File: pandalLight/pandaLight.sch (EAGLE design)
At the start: 114 parts, among them J1 PJ-037A, U13 TPD12S016PWR, U15 PMOD-2X6, U16 PMOD-2X6, U17 PLR135-T10, U18 PLT133-T10W, U20 TP10SQ, U21 TP10SQ, U22 PAN1322, U23 6SLX9TQG144, U4 FT2232HL, U5 93LC46BT-I/OT, U6 51, U7 51, U8 TPD12S016PWR, X1 USBUB-S, X2 HDMI_RECEPTICAL_A, X4 HDMI_RECEPTICAL_A, Y1 403, Y2 20Mhz

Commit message: Routed PMODs
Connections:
- net PMOD0_0: now also U23B1.IO_L32P_1
- net PMOD0_1: now also U23B1.IO_L33P_1
- net PMOD0_2: now also U23B1.IO_L34P_1
- net PMOD0_3: now also U23B1.IO_L40P_GCLK11_1
- net PMOD1_0: now also U23B1.IO_L1N_VREF_1
- net PMOD1_1: now also U23B1.IO_L32N_1
- net PMOD1_2: now also U23B1.IO_L33N_1
- net PMOD1_3: now also U23B1.IO_L34N_1
- net PMOD2_0: now also U23B0.IO_L62P_0
- net PMOD2_1: now also U23B0.IO_L63P_SCP7_0
- net PMOD2_2: now also U23B0.IO_L64P_SCP5_0
- net PMOD2_3: now also U23B0.IO_L65P_SCP3_0
- net PMOD3_0: now also U23B0.IO_L37N_GCLK12_0
- net PMOD3_1: now also U23B0.IO_L62N_VREF_0
- net PMOD3_2: now also U23B0.IO_L63N_SCP6_0
- net PMOD3_3: now also U23B0.IO_L64N_SCP4_0
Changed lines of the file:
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@@
 </instances>
 <busses>
+<bus name="PMOD2_[0..3],PMOD3_[0..3]">
+<segment>
+<wire x1="50.8" y1="48.26" x2="50.8" y2="30.48" width="0.762" layer="92"/>
+</segment>
+</bus>
 </busses>
 <nets>
@@
 </segment>
 </net>
+<net name="PMOD3_0" class="0">
+<segment>
+<pinref part="U23" gate="B0" pin="IO_L37N_GCLK12_0"/>
+<wire x1="50.8" y1="48.26" x2="25.4" y2="48.26" width="0.1524" layer="91"/>
+<label x="30.48" y="48.26" size="1.778" layer="95"/>
+</segment>
+</net>
+<net name="PMOD2_0" class="0">
+<segment>
+<pinref part="U23" gate="B0" pin="IO_L62P_0"/>
+<wire x1="50.8" y1="45.72" x2="25.4" y2="45.72" width="0.1524" layer="91"/>
+<label x="30.48" y="45.72" size="1.778" layer="95"/>
+</segment>
+</net>
+<net name="PMOD3_1" class="0">
+<segment>
+<pinref part="U23" gate="B0" pin="IO_L62N_VREF_0"/>
+<wire x1="50.8" y1="43.18" x2="25.4" y2="43.18" width="0.1524" layer="91"/>
+<label x="30.48" y="43.18" size="1.778" layer="95"/>
+</segment>
+</net>
+<net name="PMOD2_1" class="0">
+<segment>
+<pinref part="U23" gate="B0" pin="IO_L63P_SCP7_0"/>
+<wire x1="50.8" y1="40.64" x2="25.4" y2="40.64" width="0.1524" layer="91"/>
+<label x="30.48" y="40.64" size="1.778" layer="95"/>
+</segment>
+</net>
+<net name="PMOD3_2" class="0">
+<segment>
+<pinref part="U23" gate="B0" pin="IO_L63N_SCP6_0"/>
+<wire x1="50.8" y1="38.1" x2="25.4" y2="38.1" width="0.1524" layer="91"/>
+<label x="30.48" y="38.1" size="1.778" layer="95"/>
+</segment>
+</net>
+<net name="PMOD2_2" class="0">
+<segment>
+<pinref part="U23" gate="B0" pin="IO_L64P_SCP5_0"/>
+<wire x1="50.8" y1="35.56" x2="25.4" y2="35.56" width="0.1524" layer="91"/>
+<label x="30.48" y="35.56" size="1.778" layer="95"/>
+</segment>
+</net>
+<net name="PMOD3_3" class="0">
+<segment>
+<pinref part="U23" gate="B0" pin="IO_L64N_SCP4_0"/>
+<wire x1="50.8" y1="33.02" x2="25.4" y2="33.02" width="0.1524" layer="91"/>
+<label x="30.48" y="33.02" size="1.778" layer="95"/>
+</segment>
+</net>
+<net name="PMOD2_3" class="0">
+<segment>
+<pinref part="U23" gate="B0" pin="IO_L65P_SCP3_0"/>
+<wire x1="50.8" y1="30.48" x2="25.4" y2="30.48" width="0.1524" layer="91"/>
+<label x="30.48" y="30.48" size="1.778" layer="95"/>
+</segment>
+</net>
 </nets>
 </sheet>
@@
 </instances>
 <busses>
-<bus name="PMOD0_[0..3],PMOD1_[0..3],PMOD2_[0..3],PMOD3_[0..3]">
-<segment>
-<wire x1="195.58" y1="-30.48" x2="195.58" y2="10.16" width="0.762" layer="92"/>
+<bus name="PMOD0_[0..3],PMOD1_[0..3]">
+<segment>
+<wire x1="50.8" y1="50.8" x2="50.8" y2="68.58" width="0.762" layer="92"/>
 </segment>
 </bus>
@@
 </segment>
 </net>
-<net name="BT_RX" class="0">
-<segment>
-<wire x1="185.42" y1="66.04" x2="205.74" y2="66.04" width="0.1524" layer="91"/>
-<label x="187.96" y="66.04" size="1.778" layer="95"/>
-</segment>
-</net>
-<net name="BT_RTS" class="0">
-<segment>
-<wire x1="185.42" y1="73.66" x2="205.74" y2="73.66" width="0.1524" layer="91"/>
-<label x="187.96" y="73.66" size="1.778" layer="95"/>
-</segment>
-</net>
-<net name="BT_CTS" class="0">
-<segment>
-<wire x1="185.42" y1="68.58" x2="205.74" y2="68.58" width="0.1524" layer="91"/>
-<label x="187.96" y="68.58" size="1.778" layer="95"/>
-</segment>
-</net>
-<net name="BT_TX" class="0">
-<segment>
-<wire x1="185.42" y1="71.12" x2="205.74" y2="71.12" width="0.1524" layer="91"/>
-<label x="187.96" y="71.12" size="1.778" layer="95"/>
-</segment>
-</net>
-<net name="BT_WAKE" class="0">
-<segment>
-<wire x1="185.42" y1="63.5" x2="205.74" y2="63.5" width="0.1524" layer="91"/>
-<label x="187.96" y="63.5" size="1.778" layer="95"/>
-</segment>
-</net>
-<net name="BT_RESET#" class="0">
-<segment>
-<wire x1="185.42" y1="60.96" x2="205.74" y2="60.96" width="0.1524" layer="91"/>
-<label x="187.96" y="60.96" size="1.778" layer="95"/>
-</segment>
-</net>
 <net name="LEDS1_CLK_5V" class="0">
 <segment>
@@
 <pinref part="U23" gate="B1" pin="IO_L40N_GCLK10_1"/>
 <label x="30.48" y="48.26" size="1.778" layer="95"/>
+</segment>
+</net>
+<net name="PMOD1_0" class="0">
+<segment>
+<pinref part="U23" gate="B1" pin="IO_L1N_VREF_1"/>
+<wire x1="50.8" y1="68.58" x2="27.94" y2="68.58" width="0.1524" layer="91"/>
+<label x="30.48" y="68.58" size="1.778" layer="95"/>
+</segment>
+</net>
+<net name="PMOD0_0" class="0">
+<segment>
+<pinref part="U23" gate="B1" pin="IO_L32P_1"/>
+<wire x1="50.8" y1="66.04" x2="27.94" y2="66.04" width="0.1524" layer="91"/>
+<label x="30.48" y="66.04" size="1.778" layer="95"/>
+</segment>
+</net>
+<net name="PMOD1_1" class="0">
+<segment>
+<pinref part="U23" gate="B1" pin="IO_L32N_1"/>
+<wire x1="50.8" y1="63.5" x2="27.94" y2="63.5" width="0.1524" layer="91"/>
+<label x="30.48" y="63.5" size="1.778" layer="95"/>
+</segment>
+</net>
+<net name="PMOD0_1" class="0">
+<segment>
+<pinref part="U23" gate="B1" pin="IO_L33P_1"/>
+<wire x1="50.8" y1="60.96" x2="27.94" y2="60.96" width="0.1524" layer="91"/>
+<label x="30.48" y="60.96" size="1.778" layer="95"/>
+</segment>
+</net>
+<net name="PMOD1_2" class="0">
+<segment>
+<pinref part="U23" gate="B1" pin="IO_L33N_1"/>
+<wire x1="50.8" y1="58.42" x2="27.94" y2="58.42" width="0.1524" layer="91"/>
+<label x="30.48" y="58.42" size="1.778" layer="95"/>
+</segment>
+</net>
+<net name="PMOD0_2" class="0">
+<segment>
+<pinref part="U23" gate="B1" pin="IO_L34P_1"/>
+<wire x1="50.8" y1="55.88" x2="27.94" y2="55.88" width="0.1524" layer="91"/>
+<label x="30.48" y="55.88" size="1.778" layer="95"/>
+</segment>
+</net>
+<net name="PMOD1_3" class="0">
+<segment>
+<pinref part="U23" gate="B1" pin="IO_L34N_1"/>
+<wire x1="50.8" y1="53.34" x2="27.94" y2="53.34" width="0.1524" layer="91"/>
+<label x="30.48" y="53.34" size="1.778" layer="95"/>
+</segment>
+</net>
+<net name="PMOD0_3" class="0">
+<segment>
+<pinref part="U23" gate="B1" pin="IO_L40P_GCLK11_1"/>
+<wire x1="50.8" y1="50.8" x2="27.94" y2="50.8" width="0.1524" layer="91"/>
+<label x="30.48" y="50.8" size="1.778" layer="95"/>
 </segment>
 </net>
@@
 </segment>
 </net>
+<net name="BT_RX" class="0">
+<segment>
+<wire x1="53.34" y1="20.32" x2="73.66" y2="20.32" width="0.1524" layer="91"/>
+<label x="55.88" y="20.32" size="1.778" layer="95"/>
+</segment>
+</net>
+<net name="BT_RTS" class="0">
+<segment>
+<wire x1="53.34" y1="27.94" x2="73.66" y2="27.94" width="0.1524" layer="91"/>
+<label x="55.88" y="27.94" size="1.778" layer="95"/>
+</segment>
+</net>
+<net name="BT_CTS" class="0">
+<segment>
+<wire x1="53.34" y1="22.86" x2="73.66" y2="22.86" width="0.1524" layer="91"/>
+<label x="55.88" y="22.86" size="1.778" layer="95"/>
+</segment>
+</net>
+<net name="BT_TX" class="0">
+<segment>
+<wire x1="53.34" y1="25.4" x2="73.66" y2="25.4" width="0.1524" layer="91"/>
+<label x="55.88" y="25.4" size="1.778" layer="95"/>
+</segment>
+</net>
+<net name="BT_WAKE" class="0">
+<segment>
+<wire x1="53.34" y1="17.78" x2="73.66" y2="17.78" width="0.1524" layer="91"/>
+<label x="55.88" y="17.78" size="1.778" layer="95"/>
+</segment>
+</net>
+<net name="BT_RESET#" class="0">
+<segment>
+<wire x1="53.34" y1="15.24" x2="73.66" y2="15.24" width="0.1524" layer="91"/>
+<label x="55.88" y="15.24" size="1.778" layer="95"/>
+</segment>
+</net>

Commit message: Switched 3.3V with ground layer (now ground is on top); Adjusted board width to 90mm; Routed everything, about 10 airwires left!
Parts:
- removed C55, C67, C68, C70, C71: 0.1u, pandaLight:CAPACITOR0402
- removed L4: 47u, pandaLight:INDUCTOR0603
- removed LED2: Yellow, pandaLight:LED0603
- removed R23, R24, R25, R39, R48, R49: 10k, pandaLight:RESISTOR0402
- removed R26: 2.2k, pandaLight:RESISTOR0402
- removed R32: 2.4k, pandaLight:RESISTOR0402
- removed R36: 1k, pandaLight:RESISTOR0402
- removed R37: 4.7k, pandaLight:RESISTOR0402
- removed U$1: M25P40-VMN, pandaLight:M25P40-VMN
- removed U$4: TXB0104RGYR, pandaLight:TXB0104RGYR
- removed U22: PAN1322, pandaLight:PAN1322
- added C15: 0.47u, pandaLight:CAPACITOR0402
- added C16, C19: 0.1u, pandaLight:CAPACITOR0402
- added C17: 4.7u, pandaLight:CAPACITOR0603
- added C18, C23: 27p, pandaLight:CAPACITOR0402
- added L2: 2.2u, 1.3A, pandaLight:INDUCTOR1008
- added R10, R11, R6, R7: 10k, pandaLight:RESISTOR0402
- added R17: 4.7k, pandaLight:RESISTOR0402
- added R2, R3: 100k, pandaLight:RESISTOR0402
- added R4: 1k, pandaLight:RESISTOR0402
- added R9: 12k, pandaLight:RESISTOR0402
- added U12: TPD12S016PWR, pandaLight:TPD12S016PWR
- added U14: PMOD-2X6, pandaLight:PMOD-2X6
- added U3: 93LC46BT-I/OT, pandaLight:93LC46BT-I/OT
- C1, C11: value 0.47u -> 4.7u; device pandaLight:CAPACITOR0402 -> pandaLight:CAPACITOR0603; PARTNO C1005X5R0J474K050BB -> C0603C475K9PACTU
- C12, C32, C37: value 4.7u -> 0.47u; device pandaLight:CAPACITOR0603 -> pandaLight:CAPACITOR0402; PARTNO C0603C475K9PACTU -> C1005X5R0J474K050BB
- C13, C14: value 10u -> 0.47u; device pandaLight:CAPACITOR0603 -> pandaLight:CAPACITOR0402; PARTNO CL10A106MQ8NNNC -> C1005X5R0J474K050BB
- C20, C22, C27, C31, C36, C40, C41: value 0.1u -> 4.7u; device pandaLight:CAPACITOR0402 -> pandaLight:CAPACITOR0603; PARTNO CL05B104KP5NNNC -> C0603C475K9PACTU
- C24, C28, C30, C44, C50: value 4.7u -> 0.1u; device pandaLight:CAPACITOR0603 -> pandaLight:CAPACITOR0402; PARTNO C0603C475K9PACTU -> CL05B104KP5NNNC
- C3: value 4.7u -> 100u; device pandaLight:CAPACITOR0603 -> pandaLight:CAPACITOR1206; PARTNO C0603C475K9PACTU -> CL31A107MQHNNNE
- C33: value 100u -> 0.47u; device pandaLight:CAPACITOR1206 -> pandaLight:CAPACITOR0402; PARTNO CL31A107MQHNNNE -> C1005X5R0J474K050BB
- C34, C35: value 27p -> 0.1u; PARTNO CL05C270JB5NNNC -> CL05B104KP5NNNC
- C4: value 0.47u -> 100u; device pandaLight:CAPACITOR0402 -> pandaLight:CAPACITOR1206; PARTNO C1005X5R0J474K050BB -> CL31A107MQHNNNE
- C42, C43: value 0.1u -> 0.47u; PARTNO CL05B104KP5NNNC -> C1005X5R0J474K050BB
- C45, C46, C51, C52: value 0.47u -> 0.1u; PARTNO C1005X5R0J474K050BB -> CL05B104KP5NNNC
- C5: value 4.7u -> 10u; PARTNO C0603C475K9PACTU -> CL10A106MQ8NNNC
- C6: value 100u -> 10u; device pandaLight:CAPACITOR1206 -> pandaLight:CAPACITOR0603; PARTNO CL31A107MQHNNNE -> CL10A106MQ8NNNC
- JP2: value PMOD0-1_VCC_SEL -> PMOD2-3_VCC_SEL
- JP3: value PMOD2-3_VCC_SEL -> PMOD0-1_VCC_SEL
- L3: value 2.2u, 1.3A -> 47u; device pandaLight:INDUCTOR1008 -> pandaLight:INDUCTOR0603; PARTNO CIG22E1R0MNE -> GLFR1608T470M-LR
- R1: value 1k -> 100k; PARTNO ERJ-2RKF1001X -> ERJ-2RKF1003X
- R16, R5: value 100k -> 10k; PARTNO ERJ-2RKF1003X -> ERJ-2RKF1002X
- R20: value 10k -> 2.4k; PARTNO ERJ-2RKF1002X -> ERJ-2RKF2401X
- R21: value 12k -> 4.7k; PARTNO ERJ-2RKF1202X -> ERJ-2RKF1002X
- R8: value 100k -> 2.2k; PARTNO ERJ-2RKF1003X -> ERJ-2RKF2201X
- U13: value TPD12S016PWR -> M25P40-VMN; device pandaLight:TPD12S016PWR -> pandaLight:M25P40-VMN; PARTNO TPD12S016PWR -> M25P40-VMN6PB
- U16: value PMOD-2X6 -> PLR135-T10; device pandaLight:PMOD-2X6 -> pandaLight:PLR135-T10; PARTNO PPTC062LJBN-RC -> PLR135/T10
- U17: value PLR135-T10 -> PLT133-T10W; device pandaLight:PLR135-T10 -> pandaLight:PLT133-T10W; PARTNO PLR135/T10 -> PLT133/T10W
- U18: value PLT133-T10W -> TP10SQ; device pandaLight:PLT133-T10W -> pandaLight:TP10SQ; BOM (none) -> EXCLUDE; PARTNO PLT133/T10W -> *
- U20: value TP10SQ -> PAN1322; device pandaLight:TP10SQ -> pandaLight:PAN1322; BOM EXCLUDE -> (none); PARTNO * -> ENW-89841A3KF
- U5: value 93LC46BT-I/OT -> TPD12S016PWR; device pandaLight:93LC46BT-I/OT -> pandaLight:TPD12S016PWR; PARTNO 93LC46BT-I/OT -> TPD12S016PWR
- U8: value TPD12S016PWR -> TXB0104RGYR; device pandaLight:TPD12S016PWR -> pandaLight:TXB0104RGYR; PARTNO TPD12S016PWR -> (none)
- renumbered C56 to C47, C57 to C48, C58 to C49, LEDS_CON0 to U11, LEDS_CON1 to U10, R27 to R12, R28 to R13, R29 to R14, R34 to R19, R38 to R18, R40 to R15, U$2 to U1, U$3 to U9, U21 to U19, U23 to U2, X4 to X3
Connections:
- removed net +1V5: C47.1, C48.1, C49.1, U2B3.VCCO_3@0, U2B3.VCCO_3@1, U2B3.VCCO_3@2
- removed net N$33: LED2.C, U2B2.DONE_2
- removed net N$38: LED2.A, R36.1
- net +1V2: now also C10.1, C12.1, C6.1, C8.1, L1.2; no longer C2.1, C3.1, C4.1, L3.2
- net +1V8: now also C28.1, C29.1, C30.1; no longer C24.1, C25.1, C26.1
- net +3V3: now also C15.1, C16.1, C24.1, C25.1, C26.1, C31.1, C33.1, C35.1, C41.1, C47.1, C48.1, C49.1, C53.1, C54.1, C7.1, L2.2, L3.1, R1.1, R10.1, R11.2, R17.2, R20.2, R5.2, R6.2, R7.2, U12.VCCA, U13.HOLD#, U13.VCC, U13.W#, U17.VCC, U20.ONOFF, U20.VDD1, U20.VDDUART, U20.VSUPPLY@A4, U20.VSUPPLY@A5, U20.VSUPPLY@A6, U2B3.VCCO_3@0, U2B3.VCCO_3@1, U2B3.VCCO_3@2, U3.VCC, U5.VCCA, U8.OE; no longer C10.1, C12.1, C20.1, C21.1, C39.1, C44.1, C46.1, C51.1, C55.1, C68.1, C70.1, C71.1, L1.2, L4.1, R16.1, R20.1, R23.2, R24.2, R25.2, R32.2, R36.2, R37.2, R48.2, U$1.HOLD#, U$1.VCC, U$1.W#, U$4.OE, U$4.VCCA, U13.VCCA, U18.VCC, U22.ONOFF, U22.VDD1, U22.VDDUART, U22.VSUPPLY@A4, U22.VSUPPLY@A5, U22.VSUPPLY@A6, U5.VCC
- net +5V: now also C2.1, C34.1, C39.1, C4.1, C40.1, C44.1, R2.1, R3.1, R4.2, U12.VCC5V, U5.VCC5V, U8.VCCB; no longer C41.1, C54.1, C7.1, C8.1, R1.2, R5.1, R8.1, U$4.VCCB, U13.VCC5V, U8.VCC5V
- net 5V_SUP: now also C3.1; no longer C6.1
- net BT_CTS: now also U20.P0.7_UARTCTS, U2B3.IO_L2N_3; no longer U22.P0.7_UARTCTS
- net BT_RESET#: now also R21.2, U20.RESET#, U2B3.IO_L49N_3; no longer R49.2, U22.RESET#
- net BT_RTS: now also U20.P0.6_UARTRTS, U2B3.IO_L1N_VREF_3; no longer U22.P0.6_UARTRTS
- net BT_RX: now also U20.P0.5_UARTRXD, U2B3.IO_L36P_3; no longer U22.P0.5_UARTRXD
- net BT_TX: now also U20.P0.4_UARTTXD, U2B3.IO_L2P_3; no longer U22.P0.4_UARTTXD
- net BT_WAKE: now also R22.1, U20.P0.14_LPMIN, U2B3.IO_L36N_3; no longer R48.1, U22.P0.14_LPMIN
- net FPGA_CLK20: now also U2B3.IO_L83P_3; no longer U2B3.IO_L42N_GCLK24_3
- net GND: now also C15.2, C16.2, C17.2, C18.2, C19.2, C23.2, R16.1, R9.1, U12.GND@0, U12.GND@1, U12.GND@2, U13.VSS, U14.11, U14.5, U16.GND, U20.VSS@A1, U20.VSS@A11, U20.VSS@A12, U20.VSS@A7, U20.VSS@A9, U20.VSS@C8, U20.VSS@C9, U20.VSS@D7, U20.VSS@D8, U20.VSS@E8, U20.VSS@E9, U20.VSS@F1, U20.VSS@F11, U20.VSS@F12, U20.VSS@F9, U3.VSS, U5.GND@0, U5.GND@1, U5.GND@2, U8.EP, U8.GND; no longer C55.2, C67.2, C68.2, C70.2, C71.2, R39.1, R49.1, U$1.VSS, U$4.EP, U$4.GND, U13.GND@0, U13.GND@1, U13.GND@2, U16.11, U16.5, U18.GND, U22.VSS@A1, U22.VSS@A11, U22.VSS@A12, U22.VSS@A7, U22.VSS@A9, U22.VSS@C8, U22.VSS@C9, U22.VSS@D7, U22.VSS@D8, U22.VSS@E8, U22.VSS@E9, U22.VSS@F1, U22.VSS@F11, U22.VSS@F12, U22.VSS@F9, U5.VSS, U8.GND@0, U8.GND@1, U8.GND@2
- net HDMI_RX_5V: now also U5.5V_OUT; no longer C40.1, U8.5V_OUT
- net HDMI_RX_CEC: now also U5.CEC_B; no longer U8.CEC_B
- net HDMI_RX_CEC_3V3: now also U5.CEC_A; no longer U8.CEC_A
- net HDMI_RX_CLK_N: now also U5.CLK-; no longer U8.CLK-
- net HDMI_RX_CLK_P: now also U5.CLK+; no longer U8.CLK+
- net HDMI_RX_CTRL_EN: now also U5.CT_HPD, U5.LS_OE; no longer U8.CT_HPD, U8.LS_OE
- net HDMI_RX_DATA0_N: now also U5.D0-; no longer U8.D0-
- net HDMI_RX_DATA0_P: now also U5.D0+; no longer U8.D0+
- net HDMI_RX_DATA1_N: now also U5.D1-; no longer U8.D1-
- net HDMI_RX_DATA1_P: now also U5.D1+; no longer U8.D1+
- net HDMI_RX_DATA2_N: now also U5.D2-; no longer U8.D2-
- net HDMI_RX_DATA2_P: now also U5.D2+; no longer U8.D2+
- net HDMI_RX_SCL_3V3: now also U5.SCL_A; no longer U8.SCL_A
- net HDMI_RX_SCL_5V: now also U5.SCL_B; no longer U8.SCL_B
- net HDMI_RX_SDA_3V3: now also U5.SDA_A; no longer U8.SDA_A
- net HDMI_RX_SDA_5V: now also U5.SDA_B; no longer U8.SDA_B
- net HDMI_TX_5V: now also C46.1, U12.5V_OUT; no longer C53.1, U13.5V_OUT
- net HDMI_TX_CEC: now also U12.CEC_B; no longer U13.CEC_B
- net HDMI_TX_CEC_3V3: now also U12.CEC_A; no longer U13.CEC_A
- net HDMI_TX_CLK_N: now also U12.CLK-; no longer U13.CLK-
- net HDMI_TX_CLK_P: now also U12.CLK+; no longer U13.CLK+
- net HDMI_TX_CTRL_EN: now also R16.2, U12.CT_HPD, U12.LS_OE; no longer R39.2, U13.CT_HPD, U13.LS_OE
- net HDMI_TX_DATA0_N: now also U12.D0-; no longer U13.D0-
- net HDMI_TX_DATA0_P: now also U12.D0+; no longer U13.D0+
- net HDMI_TX_DATA1_N: now also U12.D1-; no longer U13.D1-
- net HDMI_TX_DATA1_P: now also U12.D1+; no longer U13.D1+
- net HDMI_TX_DATA2_N: now also U12.D2-; no longer U13.D2-
- net HDMI_TX_DATA2_P: now also U12.D2+; no longer U13.D2+
- net HDMI_TX_HPD_5V: now also U12.HPD_B; no longer U13.HPD_B
- net HDMI_TX_SCL_3V3: now also U12.SCL_A; no longer U13.SCL_A
- net HDMI_TX_SCL_5V: now also U12.SCL_B; no longer U13.SCL_B
- net HDMI_TX_SDA_3V3: now also U12.SDA_A; no longer U13.SDA_A
- net HDMI_TX_SDA_5V: now also U12.SDA_B; no longer U13.SDA_B
- net LEDS0_CLK: now also U8.A4; no longer U$4.A4
- net LEDS0_CLK_5V: now also U8.B4; no longer U$4.B4
- net LEDS0_DATA: now also U8.A1; no longer U$4.A1
- net LEDS0_DATA_5V: now also U8.B1; no longer U$4.B1
- net LEDS1_CLK: now also U8.A2; no longer U$4.A2
- net LEDS1_CLK_5V: now also U8.B2; no longer U$4.B2
- net LEDS1_DATA: now also U8.A3; no longer U$4.A3
- net LEDS1_DATA_5V: now also U8.B3; no longer U$4.B3
- net N$1: now also C23.1; no longer C35.1
- net N$10: now also R8.2, U3.DI; no longer R26.2, U5.DI
- net N$11: now also R9.2; no longer R21.2
- net N$12: now also R7.1, R8.1, U3.DO; no longer R25.1, R26.1, U5.DO
- net N$13: now also R10.2; no longer R20.2
- net N$19: now also U20.P0.12_SDA0; no longer U22.P0.12_SDA0
- net N$25: now also R3.2; no longer R8.2
- net N$27: now also R1.2; no longer R16.2
- net N$28: now also C20.1, C21.1, FB1.2; no longer C30.1, C31.1, FB2.2
- net N$29: now also U18.TP, U20.P0.13_SCL0; no longer U20.TP, U22.P0.13_SCL0
- net N$31: now also C17.1, C19.1, FB2.2; no longer C28.1, C29.1, FB1.2
- net N$34: now also R17.1; no longer R37.1
- net N$36: now also C51.1, L3.2, U16.VCC; no longer C67.1, L4.2, U17.VCC
- net N$4: now also R2.2; no longer R5.2
- net N$40: now also U13.DQ0; no longer U$1.DQ0
- net N$41: now also R20.1, U13.S#; no longer R32.1, U$1.S#
- net N$42: now also U13.C; no longer U$1.C
- net N$43: now also U13.DQ1; no longer U$1.DQ1
- net N$47: now also R4.1; no longer R1.1
- net N$49: now also JP2.2, U14.12, U14.6; no longer JP3.2, U16.12, U16.6
- net N$5: now also C18.1; no longer C34.1
- net N$51: now also JP3.2; no longer JP2.2
- net N$6: now also R5.1, U3.CS; no longer R22.1, U5.CS
- net N$9: now also R6.1, U3.CLK; no longer R23.1, U5.CLK
- net PMOD2_0: now also U14.1; no longer U16.1
- net PMOD2_1: now also U14.2; no longer U16.2
- net PMOD2_2: now also U14.3; no longer U16.3
- net PMOD2_3: now also U14.4; no longer U16.4
- net PMOD3_0: now also U14.7; no longer U16.7
- net PMOD3_1: now also U14.8; no longer U16.8
- net PMOD3_2: now also U14.9; no longer U16.9
- net PMOD3_3: now also U14.10; no longer U16.10
- net SW1: now also L2.1; no longer L1.1
- net SW2: now also L1.1; no longer L3.1
- net TOS_IN: now also U16.VOUT, U2B3.IO_L83N_VREF_3; no longer U17.VOUT, U2B0.IO_L37P_GCLK13_0
- net TOS_OUT: now also U17.VIN, U2B3.IO_L1P_3; no longer U18.VIN, U2B2.IO_L62P_D5_2
- net USB_PWRSAVE#: now also R11.1; no longer R24.1
- net USB_VBUS: no longer C33.1

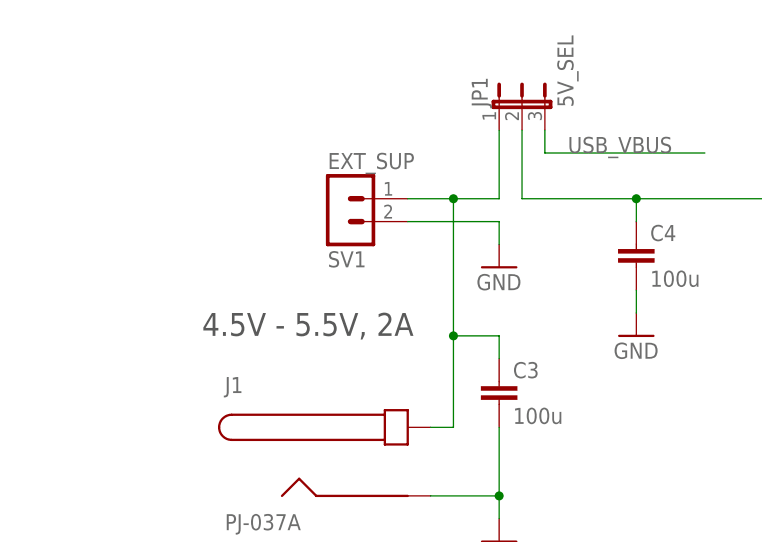
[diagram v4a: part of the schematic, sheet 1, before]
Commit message: No more airwires! Added ESD protection at 5V_SUP
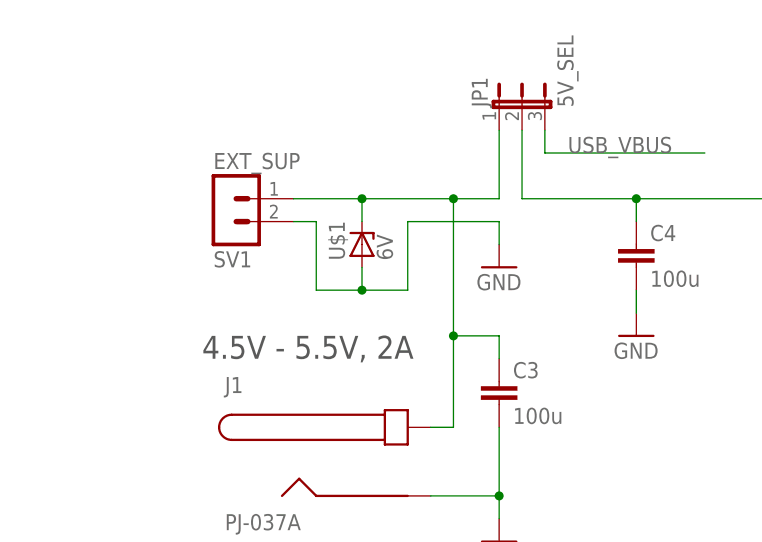
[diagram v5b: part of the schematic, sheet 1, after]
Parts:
- added U$1: 6V, pandaLight:ZENER_DIODE
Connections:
- net 5V_SUP: now also U$1.C
- net GND: now also U$1.A
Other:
- moved on the sheet: SV1
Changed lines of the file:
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@@
 <part name="PS42" library="pandaLight" deviceset="+5V" device=""/>
 <part name="GND31" library="pandaLight" deviceset="GND" device=""/>
+<part name="U$1" library="pandaLight" deviceset="ZENER_DIODE" device="" value="6V"/>
 </parts>
 <sheets>
@@
 <description>Power</description>
 <plain>
-<text x="22.86" y="96.52" size="2.54" layer="97">4.5V - 5.5V, 2A</text>
+<text x="22.86" y="93.98" size="2.54" layer="97">4.5V - 5.5V, 2A</text>
 <text x="119.38" y="48.26" size="2.54" layer="97">3.3V, 0.8A</text>
 <text x="119.38" y="33.02" size="2.54" layer="97">1.2V, 0.8A</text>
@@
 </instance>
 <instance part="GND3" gate="1" x="55.88" y="104.14"/>
-<instance part="SV1" gate="G$1" x="38.1" y="109.22" rot="MR180">
-<attribute name="PARTNO" x="38.1" y="109.22" size="1.778" layer="96" display="off"/>
-<attribute name="BOM" x="38.1" y="109.22" size="1.778" layer="96" display="off"/>
+<instance part="SV1" gate="G$1" x="25.4" y="109.22" rot="MR180">
+<attribute name="PARTNO" x="25.4" y="109.22" size="1.778" layer="96" display="off"/>
+<attribute name="BOM" x="25.4" y="109.22" size="1.778" layer="96" display="off"/>
 </instance>
 <instance part="GND2" gate="1" x="55.88" y="73.66"/>
@@
 <attribute name="PARTNO" x="185.42" y="81.28" size="1.778" layer="96" display="off"/>
 </instance>
+<instance part="U$1" gate="G$1" x="40.64" y="106.68" rot="R90"/>
 </instances>
 <busses>
@@
 <pinref part="SV1" gate="G$1" pin="2"/>
 <pinref part="GND3" gate="1" pin="GND"/>
+<wire x1="33.02" y1="109.22" x2="35.56" y2="109.22" width="0.1524" layer="91"/>
+<wire x1="35.56" y1="109.22" x2="35.56" y2="101.6" width="0.1524" layer="91"/>
+<wire x1="35.56" y1="101.6" x2="40.64" y2="101.6" width="0.1524" layer="91"/>
+<wire x1="40.64" y1="101.6" x2="45.72" y2="101.6" width="0.1524" layer="91"/>
+<wire x1="45.72" y1="101.6" x2="45.72" y2="109.22" width="0.1524" layer="91"/>
 <wire x1="45.72" y1="109.22" x2="55.88" y2="109.22" width="0.1524" layer="91"/>
 <wire x1="55.88" y1="109.22" x2="55.88" y2="106.68" width="0.1524" layer="91"/>
+<pinref part="U$1" gate="G$1" pin="A"/>
+<wire x1="40.64" y1="101.6" x2="40.64" y2="104.14" width="0.1524" layer="91"/>
+<junction x="40.64" y="101.6"/>
 </segment>
 <segment>
@@
 <wire x1="55.88" y1="111.76" x2="50.8" y2="111.76" width="0.1524" layer="91"/>
 <pinref part="J1" gate="G$1" pin="CENTER"/>
-<wire x1="50.8" y1="111.76" x2="45.72" y2="111.76" width="0.1524" layer="91"/>
+<wire x1="50.8" y1="111.76" x2="40.64" y2="111.76" width="0.1524" layer="91"/>
+<wire x1="40.64" y1="111.76" x2="33.02" y2="111.76" width="0.1524" layer="91"/>
 <wire x1="48.26" y1="86.36" x2="50.8" y2="86.36" width="0.1524" layer="91"/>
 <wire x1="50.8" y1="86.36" x2="50.8" y2="96.52" width="0.1524" layer="91"/>
@@
 <wire x1="55.88" y1="96.52" x2="55.88" y2="93.98" width="0.1524" layer="91"/>
 <junction x="50.8" y="96.52"/>
-</segment>
-</net>
+<pinref part="U$1" gate="G$1" pin="C"/>
+<wire x1="40.64" y1="109.22" x2="40.64" y2="111.76" width="0.1524" layer="91"/>
+<junction x="40.64" y="111.76"/>
+</segment>
+</net>
